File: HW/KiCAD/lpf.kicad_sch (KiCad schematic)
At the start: 30 parts, among them U41 NE5532, U44 NE5532

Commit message: some eidts, remove com
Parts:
- renumbered C181 to C170, C182 to C171, C199 to C172, C180 to C173, C201 to C174, C184 to C175, JP8 to JP2, L22 to L15, L17 to L16, R133 to R105, R134 to R106, R171 to R107, R119 to R108, R120 to R109, R129 to R110, R121 to R111, R130 to R112, R122 to R113, R123 to R114, R124 to R115, R131 to R116, R125 to R117, R132 to R118, R126 to R119, R127 to R120, R128 to R121, U41 to U32, U44 to U32, U44 to U33

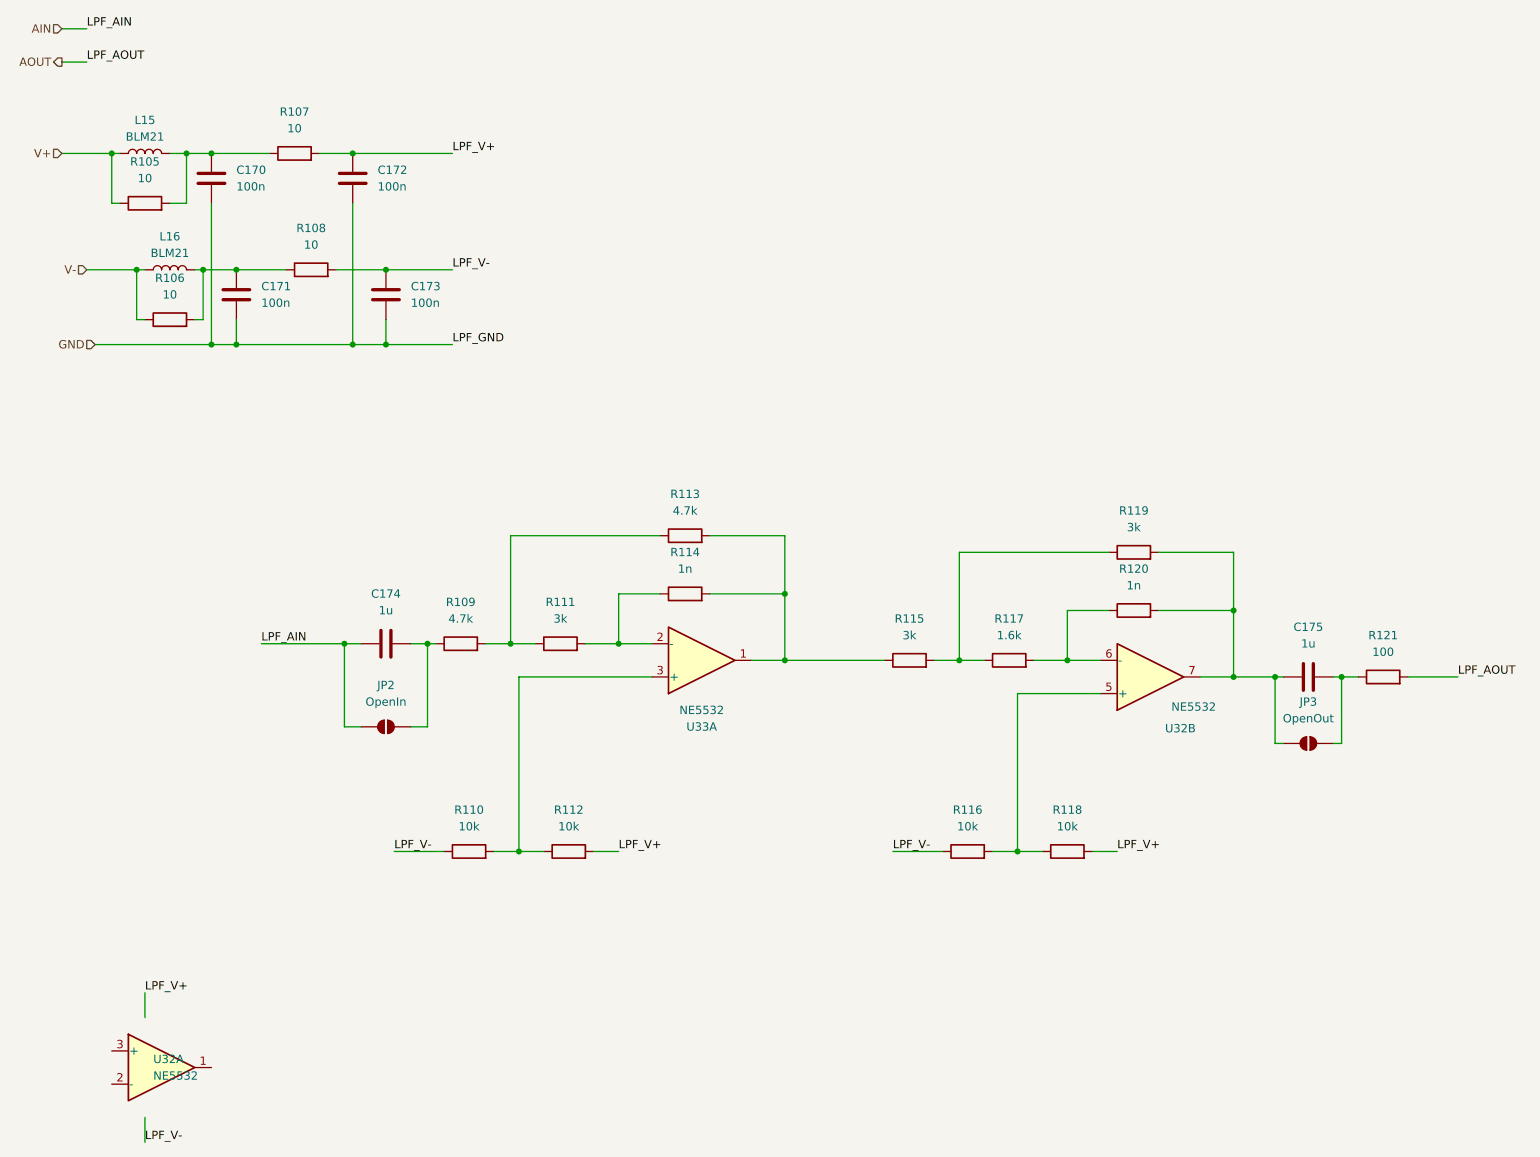
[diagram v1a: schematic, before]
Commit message: some edits, add HP amp
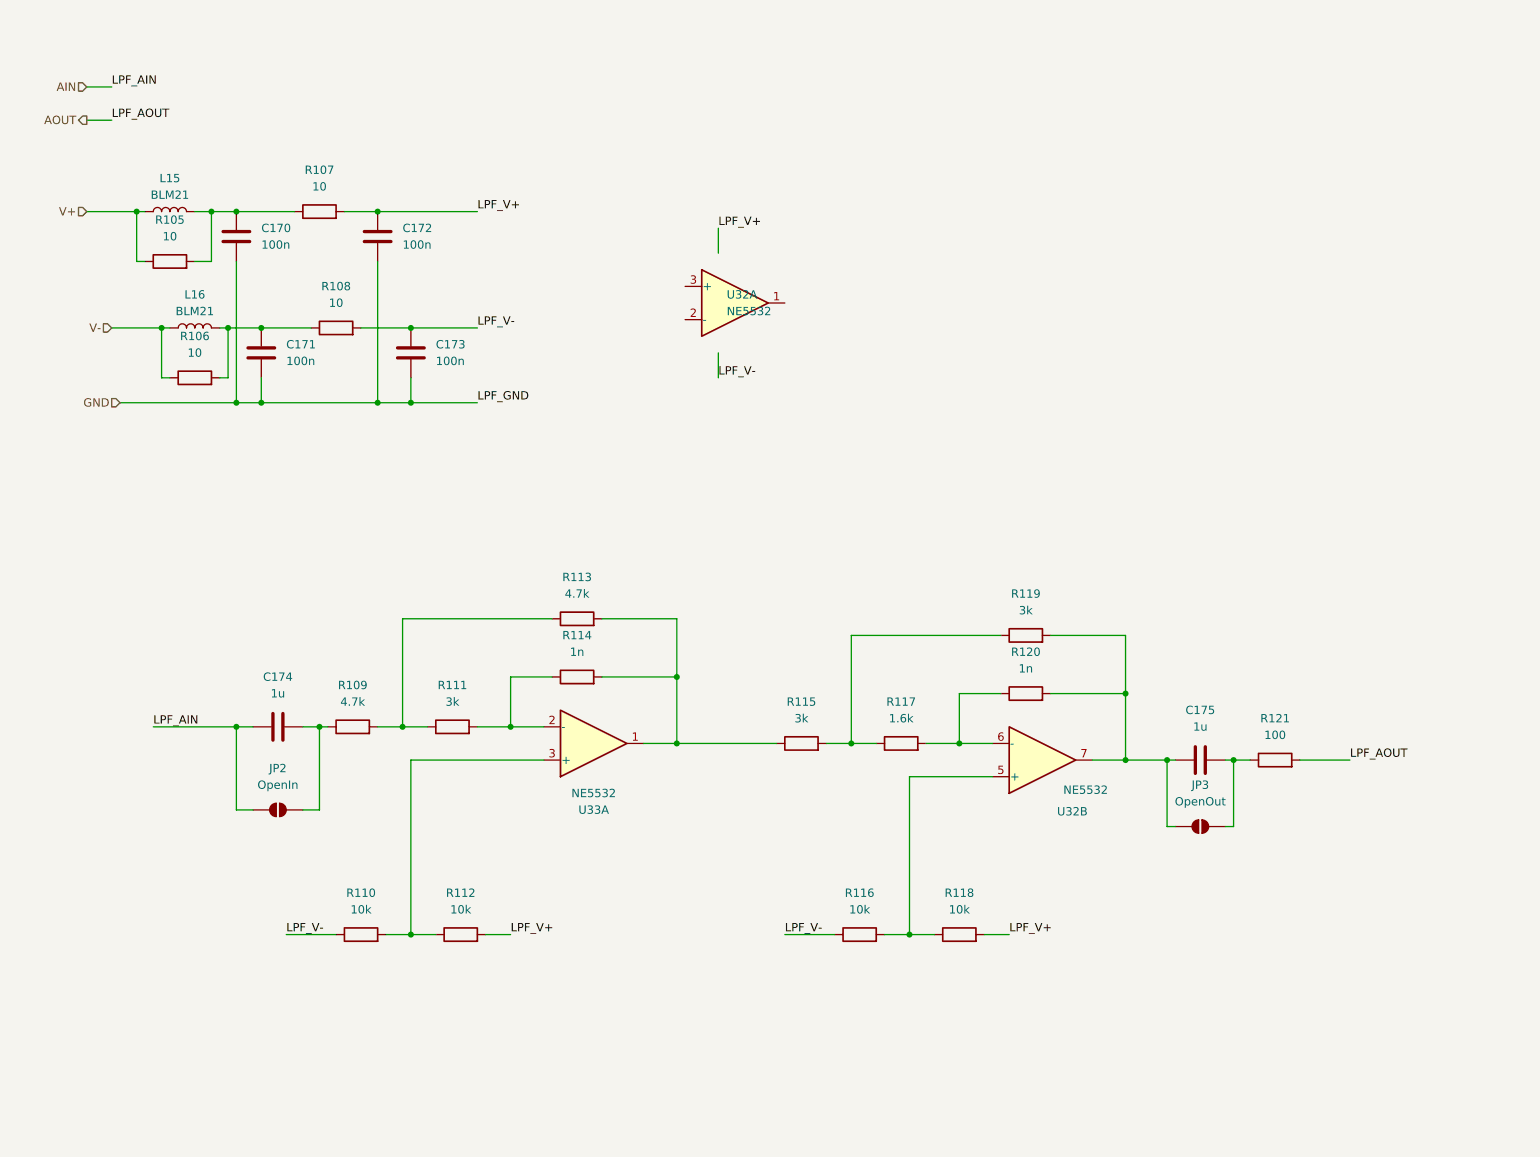
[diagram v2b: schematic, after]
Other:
- moved on the sheet: C170, C171, C172, C173, C174, C175, JP2, JP3, L15, L16, R105, R106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
